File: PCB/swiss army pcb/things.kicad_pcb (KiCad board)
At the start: 2 copper layers, 54.6 x 89.5 mm, 44 parts, among them J1 Microphone, J2 Mic, J3 Headphone, J4 Speaker Left, J5 Speaker Right, J6 Battery, J7 Conn_01x07_Pin, J8 I2C Display, SW1 SW_SPDT, SW2 SW_Push, SW3 SW_Push, SW4 SW_Push, SW5 SW_Push, U1 MCP6002-xSN, U2 TPA2012D2RTJT, U3 Pico

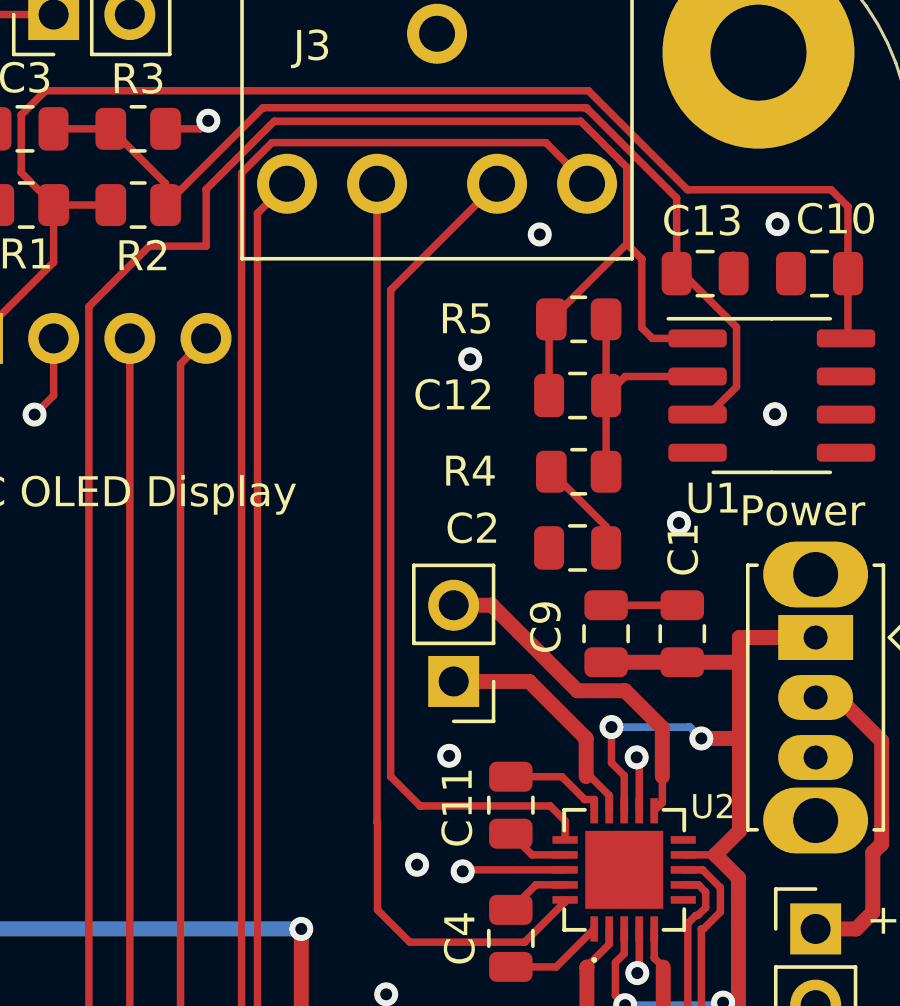
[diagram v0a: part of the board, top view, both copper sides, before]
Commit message: Update docs for FM radio
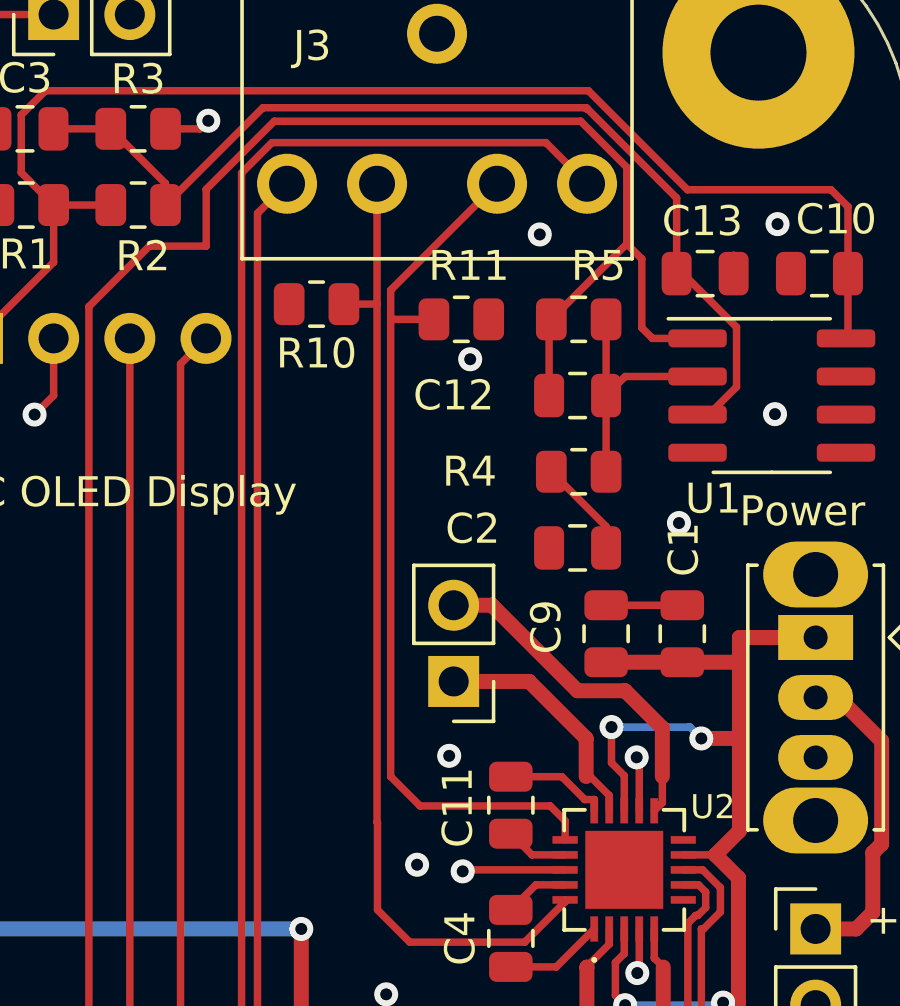
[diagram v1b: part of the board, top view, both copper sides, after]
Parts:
- added R10: 1K, Resistor_SMD:R_0805_2012Metric, F.Cu at (135.1, 113.8)
- added R11: 1K, Resistor_SMD:R_0805_2012Metric, F.Cu at (140.0, 114.3)
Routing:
- net Net-(U2-INR+): track 28.3 -> 29.7 mm
- net Net-(U2-INL+): track 31.5 -> 32.6 mm
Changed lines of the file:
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@@
     (property "ki_keywords" "R res resistor")
     (attr smd)
-    (fp_text reference "R5" (at 3.7475 0) (layer "F.SilkS")
+    (fp_text reference "R5" (at -0.6585 1.778) (layer "F.SilkS")
         (effects (font (size 1 1) (thickness 0.15)))
     )
@@
       (net 2 "GND") (pintype "passive"))
     (model "${KICAD6_3DMODEL_DIR}/Capacitor_SMD.3dshapes/C_0805_2012Metric.wrl"
+      (offset (xyz 0 0 0))
+      (scale (xyz 1 1 1))
+      (rotate (xyz 0 0 0))
+    )
+  )
+  (footprint "Resistor_SMD:R_0805_2012Metric" (layer "F.Cu")
+    (at 135.128 113.792 180)
+    (descr "Resistor SMD 0805 (2012 Metric), square (rectangular) end terminal, IPC_7351 nominal, (Body size source: IPC-SM-782 page 72, https://www.pcb-3d.com/wordpress/wp-content/uploads/ipc-sm-782a_amendment_1_and_2.pdf), generated with kicad-footprint-generator")
+    (tags "resistor")
+    (property "Sheetfile" "audio.kicad_sch")
+    (property "Sheetname" "Audio")
+    (property "ki_description" "Resistor")
+    (property "ki_keywords" "R res resistor")
+    (attr smd)
+    (fp_text reference "R10" (at 0 -1.65) (layer "F.SilkS")
+        (effects (font (size 1 1) (thickness 0.15)))
+    )
+    (fp_text value "1K" (at 0 1.65) (layer "F.Fab")
+        (effects (font (size 1 1) (thickness 0.15)))
+    )
+    (fp_text user "${REFERENCE}" (at 0 0) (layer "F.Fab")
+        (effects (font (size 0.5 0.5) (thickness 0.08)))
+    )
+    (fp_line (start -0.227064 -0.735) (end 0.227064 -0.735)
+      (stroke (width 0.12) (type solid)) (layer "F.SilkS"))
+    (fp_line (start -0.227064 0.735) (end 0.227064 0.735)
+      (stroke (width 0.12) (type solid)) (layer "F.SilkS"))
+    (fp_line (start -1.68 -0.95) (end 1.68 -0.95)
+      (stroke (width 0.05) (type solid)) (layer "F.CrtYd"))
+    (fp_line (start -1.68 0.95) (end -1.68 -0.95)
+      (stroke (width 0.05) (type solid)) (layer "F.CrtYd"))
+    (fp_line (start 1.68 -0.95) (end 1.68 0.95)
+      (stroke (width 0.05) (type solid)) (layer "F.CrtYd"))
+    (fp_line (start 1.68 0.95) (end -1.68 0.95)
+      (stroke (width 0.05) (type solid)) (layer "F.CrtYd"))
+    (fp_line (start -1 -0.625) (end 1 -0.625)
+      (stroke (width 0.1) (type solid)) (layer "F.Fab"))
+    (fp_line (start -1 0.625) (end -1 -0.625)
+      (stroke (width 0.1) (type solid)) (layer "F.Fab"))
+    (fp_line (start 1 -0.625) (end 1 0.625)
+      (stroke (width 0.1) (type solid)) (layer "F.Fab"))
+    (fp_line (start 1 0.625) (end -1 0.625)
+      (stroke (width 0.1) (type solid)) (layer "F.Fab"))
+    (pad "1" smd roundrect (at -0.9125 0 180) (size 1.025 1.4) (layers "F.Cu" "F.Paste" "F.Mask") (roundrect_rratio 0.243902)
+      (net 57 "Net-(U2-INL+)") (pintype "passive"))
+    (pad "2" smd roundrect (at 0.9125 0 180) (size 1.025 1.4) (layers "F.Cu" "F.Paste" "F.Mask") (roundrect_rratio 0.243902)
+      (net 2 "GND") (pintype "passive"))
+    (model "${KICAD6_3DMODEL_DIR}/Resistor_SMD.3dshapes/R_0805_2012Metric.wrl"
       (offset (xyz 0 0 0))
       (scale (xyz 1 1 1))
@@
     (pad "2" smd roundrect (at 0.9125 0) (size 1.025 1.4) (layers "F.Cu" "F.Paste" "F.Mask") (roundrect_rratio 0.243902439)
       (net 59 "Net-(C6-Pad1)") (pintype "passive"))
+    (model "${KICAD6_3DMODEL_DIR}/Resistor_SMD.3dshapes/R_0805_2012Metric.wrl"
+      (offset (xyz 0 0 0))
+      (scale (xyz 1 1 1))
+      (rotate (xyz 0 0 0))
+    )
+  )
+  (footprint "Resistor_SMD:R_0805_2012Metric" (layer "F.Cu")
+    (at 139.954 114.3)
+    (descr "Resistor SMD 0805 (2012 Metric), square (rectangular) end terminal, IPC_7351 nominal, (Body size source: IPC-SM-782 page 72, https://www.pcb-3d.com/wordpress/wp-content/uploads/ipc-sm-782a_amendment_1_and_2.pdf), generated with kicad-footprint-generator")
+    (tags "resistor")
+    (property "Sheetfile" "audio.kicad_sch")
+    (property "Sheetname" "Audio")
+    (property "ki_description" "Resistor")
+    (property "ki_keywords" "R res resistor")
+    (attr smd)
+    (fp_text reference "R11" (at 0.254 -1.778) (layer "F.SilkS")
+        (effects (font (size 1 1) (thickness 0.15)))
+    )
+    (fp_text value "1K" (at 0 1.65) (layer "F.Fab")
+        (effects (font (size 1 1) (thickness 0.15)))
+    )
+    (fp_text user "${REFERENCE}" (at 0 0) (layer "F.Fab")
+        (effects (font (size 0.5 0.5) (thickness 0.08)))
+    )
+    (fp_line (start -0.227064 -0.735) (end 0.227064 -0.735)
+      (stroke (width 0.12) (type solid)) (layer "F.SilkS"))
+    (fp_line (start -0.227064 0.735) (end 0.227064 0.735)
+      (stroke (width 0.12) (type solid)) (layer "F.SilkS"))
+    (fp_line (start -1.68 -0.95) (end 1.68 -0.95)
+      (stroke (width 0.05) (type solid)) (layer "F.CrtYd"))
+    (fp_line (start -1.68 0.95) (end -1.68 -0.95)
+      (stroke (width 0.05) (type solid)) (layer "F.CrtYd"))
+    (fp_line (start 1.68 -0.95) (end 1.68 0.95)
+      (stroke (width 0.05) (type solid)) (layer "F.CrtYd"))
+    (fp_line (start 1.68 0.95) (end -1.68 0.95)
+      (stroke (width 0.05) (type solid)) (layer "F.CrtYd"))
+    (fp_line (start -1 -0.625) (end 1 -0.625)
+      (stroke (width 0.1) (type solid)) (layer "F.Fab"))
+    (fp_line (start -1 0.625) (end -1 -0.625)
+      (stroke (width 0.1) (type solid)) (layer "F.Fab"))
+    (fp_line (start 1 -0.625) (end 1 0.625)
+      (stroke (width 0.1) (type solid)) (layer "F.Fab"))
+    (fp_line (start 1 0.625) (end -1 0.625)
+      (stroke (width 0.1) (type solid)) (layer "F.Fab"))
+    (pad "1" smd roundrect (at -0.9125 0) (size 1.025 1.4) (layers "F.Cu" "F.Paste" "F.Mask") (roundrect_rratio 0.243902)
+      (net 56 "Net-(U2-INR+)") (pintype "passive"))
+    (pad "2" smd roundrect (at 0.9125 0) (size 1.025 1.4) (layers "F.Cu" "F.Paste" "F.Mask") (roundrect_rratio 0.243902)
+      (net 2 "GND") (pintype "passive"))
     (model "${KICAD6_3DMODEL_DIR}/Resistor_SMD.3dshapes/R_0805_2012Metric.wrl"
       (offset (xyz 0 0 0))
@@
   (segment (start 144.78 121.92) (end 144.78 121.205) (width 0.25) (layer "F.Cu") (net 55))
   (segment (start 144.78 121.205) (end 142.955 119.38) (width 0.25) (layer "F.Cu") (net 55))
+  (segment (start 137.6 114.3) (end 137.6 129.54) (width 0.25) (layer "F.Cu") (net 56))
   (segment (start 142.92 130.52) (end 143.415 131.015) (width 0.25) (layer "F.Cu") (net 56))
   (segment (start 141.145 109.78) (end 137.6 113.325) (width 0.25) (layer "F.Cu") (net 56))
+  (segment (start 139.0415 114.3) (end 137.6 114.3) (width 0.25) (layer "F.Cu") (net 56))
+  (segment (start 137.6 113.325) (end 137.6 114.3) (width 0.25) (layer "F.Cu") (net 56))
   (segment (start 143.415 131.015) (end 143.415 131.65) (width 0.25) (layer "F.Cu") (net 56))
-  (segment (start 137.6 113.325) (end 137.6 129.54) (width 0.25) (layer "F.Cu") (net 56))
   (segment (start 138.58 130.52) (end 142.92 130.52) (width 0.25) (layer "F.Cu") (net 56))
   (segment (start 137.6 129.54) (end 138.58 130.52) (width 0.25) (layer "F.Cu") (net 56))
@@
   (segment (start 142.068173 135.06) (end 138.235 135.06) (width 0.25) (layer "F.Cu") (net 57))
   (segment (start 143.415 133.713173) (end 142.068173 135.06) (width 0.25) (layer "F.Cu") (net 57))
-  (segment (start 137.145 131.063173) (end 137.145 109.78) (width 0.25) (layer "F.Cu") (net 57))
+  (segment (start 137.145 113.792) (end 137.145 109.78) (width 0.25) (layer "F.Cu") (net 57))
   (segment (start 143.415 133.65) (end 143.415 133.713173) (width 0.25) (layer "F.Cu") (net 57))
+  (segment (start 136.0405 113.792) (end 137.145 113.792) (width 0.25) (layer "F.Cu") (net 57))
   (segment (start 138.235 135.06) (end 137.16 133.985) (width 0.25) (layer "F.Cu") (net 57))
   (segment (start 137.16 133.985) (end 137.16 131.078173) (width 0.25) (layer "F.Cu") (net 57))
+  (segment (start 137.145 131.063173) (end 137.145 113.792) (width 0.25) (layer "F.Cu") (net 57))
   (segment (start 135.78 182.84) (end 135.24 182.3) (width 0.25) (layer "F.Cu") (net 58))
   (segment (start 131.895 182.595) (end 131.895 184.15) (width 0.25) (layer "F.Cu") (net 58))
